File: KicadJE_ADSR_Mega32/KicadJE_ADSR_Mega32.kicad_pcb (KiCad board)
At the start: 2 copper layers, 100 x 100 mm, 212 parts, among them J101 ADSR1, J102 ADSR2, J103 ADSR1, J104 ADSR2, J105 ADSR1-G8, J106 ADSR2-G8, J107 ADSR4-G8, J108 ADSR3-G8, J201 AVR-ISP-6, J202 UART, J301 In, J302 +5V reg/doepfer, J303 Out, J304 CV_time, J305 CV doepfer, J401 CV, J402 FM, J403 Trigger, J404 Out, J405 SQ Out, J406 Sine Out, P101 Doepfer_Power_16pin, P302 Doepfer_Power_16pin, P401 Doepfer_Power_16pin, Q301 BC337, Q302 PZT2222A, Q401 UMX1N, Q402 MMBT2222A, Q403 MMBT2222A, Q404 MMBT2222A, Q405 MMBT2222A, SW401 LFO, SW402 SQ_Source, U201 ATmega32A-AU, U301 L78L05_TO92, U302 PT2399, U401 TL074, U402 74HC00, U403 TL072, Y201 16MHz

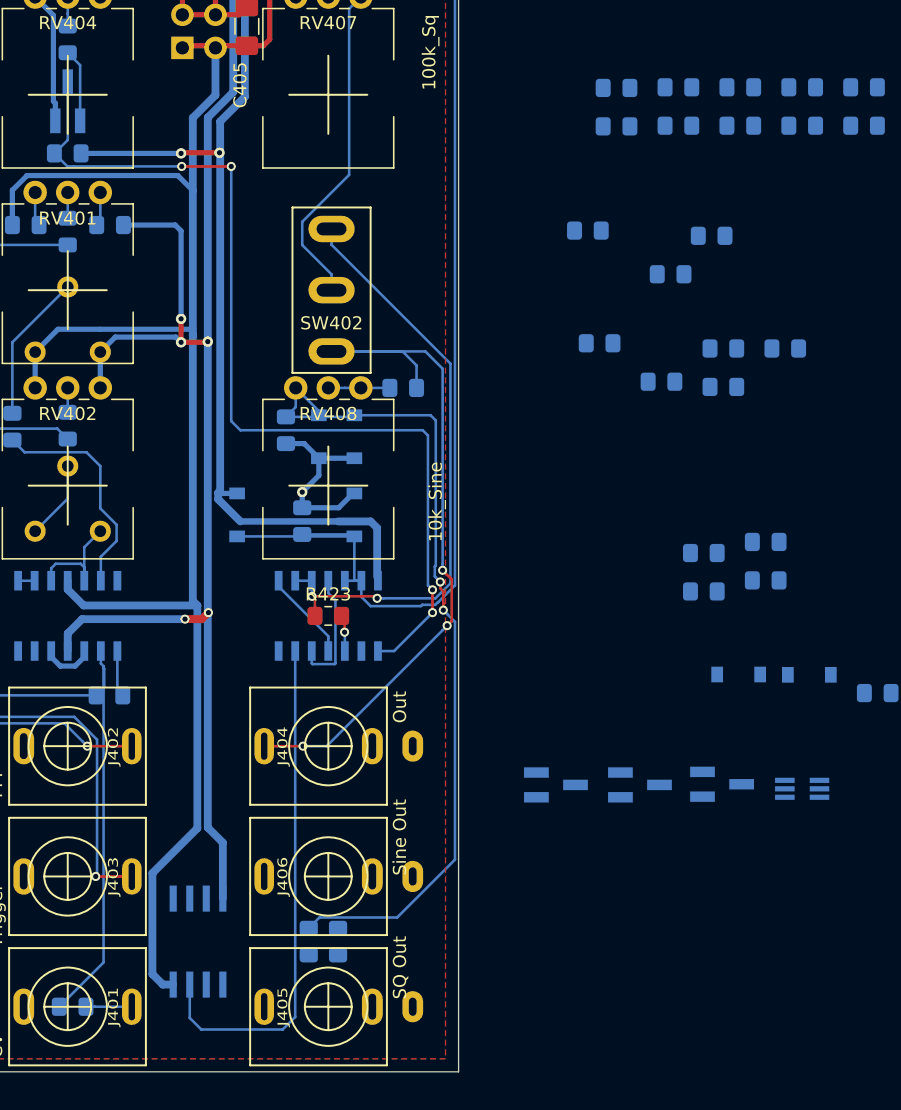
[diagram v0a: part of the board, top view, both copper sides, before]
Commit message: Square out - and decoupling
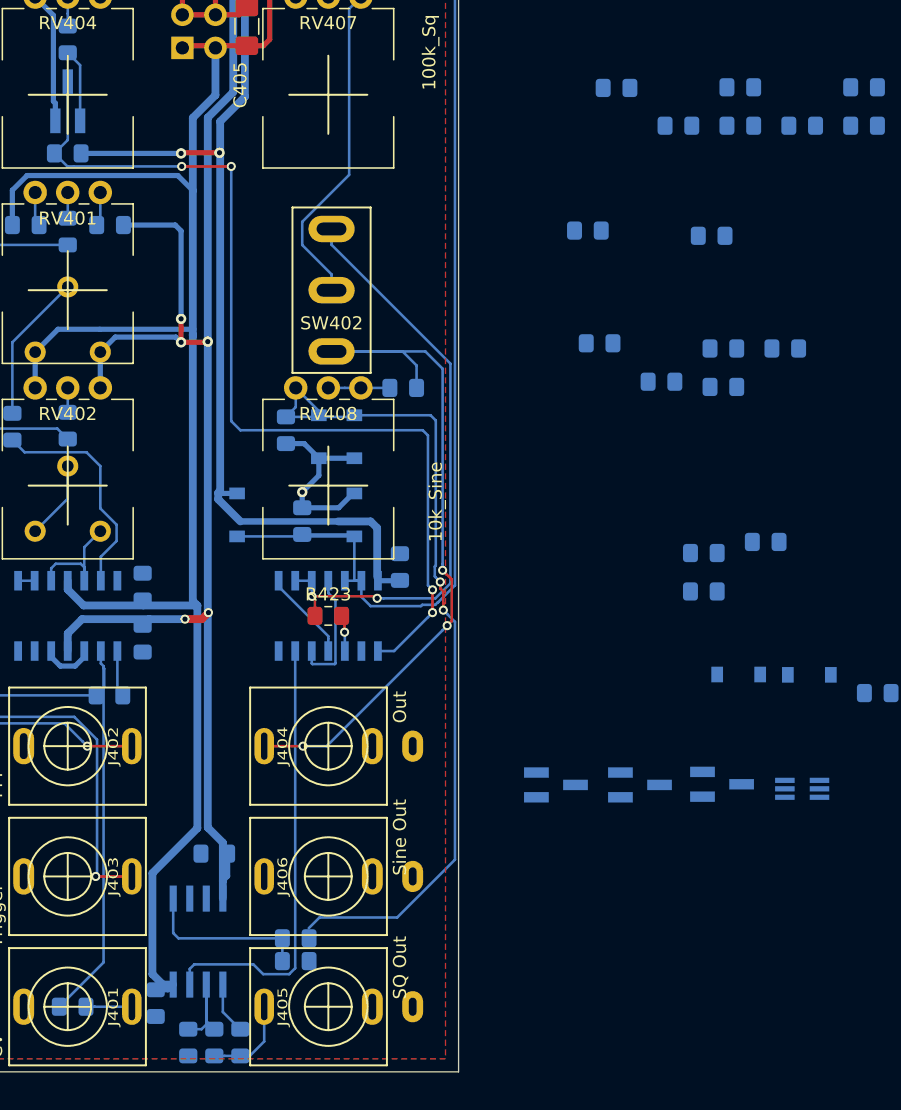
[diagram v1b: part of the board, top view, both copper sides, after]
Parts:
- added C412: 100n, Capacitor_SMD:C_0805_2012Metric_Pad1.15x1.40mm_HandSolder, B.Cu at (131.2, 133.2)
- added C413: 100n, Capacitor_SMD:C_0805_2012Metric_Pad1.15x1.40mm_HandSolder, B.Cu at (126.8, 144.7)
- added R435: 10k, Resistor_SMD:R_0805_2012Metric_Pad1.15x1.40mm_HandSolder, B.Cu at (131.2, 147.8)
- R416: value 4k7 -> 10k
- RV405: value 10k_offset -> 10k_Offset_out
- moved R426 85.1 mm to (133.2, 147.8), turned to 90 degrees
- moved R416 82.4 mm to (129.2, 147.8), turned to 90 degrees
- moved C408 53.6 mm to (125.8, 116.8), turned to 90 degrees
- moved C406 47.8 mm to (125.8, 112.8), turned to 270 degrees
- moved C404 30.6 mm to (145.5, 111.2), turned to 270 degrees
- moved R433 3.58 mm to (137.5, 141.5), turned to 180 degrees
- moved R432 1.03 mm to (137.5, 139.8), turned to 180 degrees
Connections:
- R416 pad 1: Net-(R416-Pad1) -> GNDA
- R416 pad 2: VCO_SQ_Out -> Net-(R416-Pad2)
- U403 pad 2: Net-(R416-Pad1) -> Net-(R416-Pad2)
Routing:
- net Net-(R432-Pad2): track 0.00 -> 12.9 mm
- net Net-(R416-Pad2): track 0.00 -> 8.28 mm
- net VCO_SQ_Out: track 0.00 -> 6.96 mm
- net Net-(U402-Pad6): track 39.5 -> 34.3 mm
- net Net-(R426-Pad2): track 0.00 -> 4.03 mm
- net +12V: track 129.1 -> 132.1 mm
- net -12V: track 150.3 -> 152.2 mm
- net +5VA: track 125.5 -> 127.2 mm

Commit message: Most of the oscillator
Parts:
- Q403, Q404, R420, R424: moved to F.Cu
- moved R419 70.8 mm to (115.2, 120.2), turned to 180 degrees
- moved Q401 63.7 mm to (114.0, 115.2), turned to 270 degrees
- moved C403 63.1 mm to (118.8, 120.2), turned to 180 degrees
- moved R424 54.3 mm to (137.0, 114.7), turned to 270 degrees
- moved R425 49.8 mm to (122.2, 110.5), turned to 180 degrees
- moved R421 48.3 mm to (145.5, 115.0), turned to 90 degrees
- moved R417 46.0 mm to (123.0, 120.2)
- moved D402 45.0 mm to (132.0, 117.5), turned to 270 degrees
- moved C402 43.3 mm to (125.8, 109.0), turned to 270 degrees
- moved D401 40.1 mm to (132.0, 112.8), turned to 270 degrees
- moved R420 35.1 mm to (135.2, 114.8), turned to 90 degrees
- moved Q404 32.2 mm to (139.5, 118.2)
- moved Q403 31.5 mm to (134.0, 118.2)
- moved Q405 20.5 mm to (154.0, 107.8)
- moved C409 19.6 mm to (154.5, 104.2), turned to 180 degrees
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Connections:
- C406 pad 1: GND -> GNDA
- C408 pad 1: GND -> GNDA
- C412 pad 1: GND -> GNDA
- C413 pad 1: GND -> GNDA
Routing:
- net GNDA: track 115.9 -> 153.0 mm, vias 15 -> 23
- net /AJ_VCO_Formant/b1: track 0.00 -> 21.0 mm
- net Net-(D401-Pad2): track 0.00 -> 19.0 mm, vias 0 -> 2
- net /AJ_VCO_Formant/c1: track 0.00 -> 16.1 mm
- net +5VA: track 127.2 -> 141.5 mm, vias 2 -> 3
- net Net-(Q404-Pad3): track 0.00 -> 7.49 mm, vias 0 -> 1
- net /AJ_VCO_Formant/e1: track 0.00 -> 7.48 mm
- net Net-(R425-Pad2): track 1.27 -> 6.34 mm
- net VCO_Exp: track 9.09 -> 13.6 mm
- net Net-(Q403-Pad3): track 0.00 -> 4.34 mm
- net Net-(C403-Pad2): track 0.00 -> 4.14 mm
- net Net-(Q404-Pad1): track 0.00 -> 4.01 mm
- net Net-(R413-Pad2): track 3.57 -> 7.52 mm
- net Net-(C402-Pad1): track 17.4 -> 21.1 mm
- net Net-(C402-Pad2): track 0.00 -> 3.37 mm
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
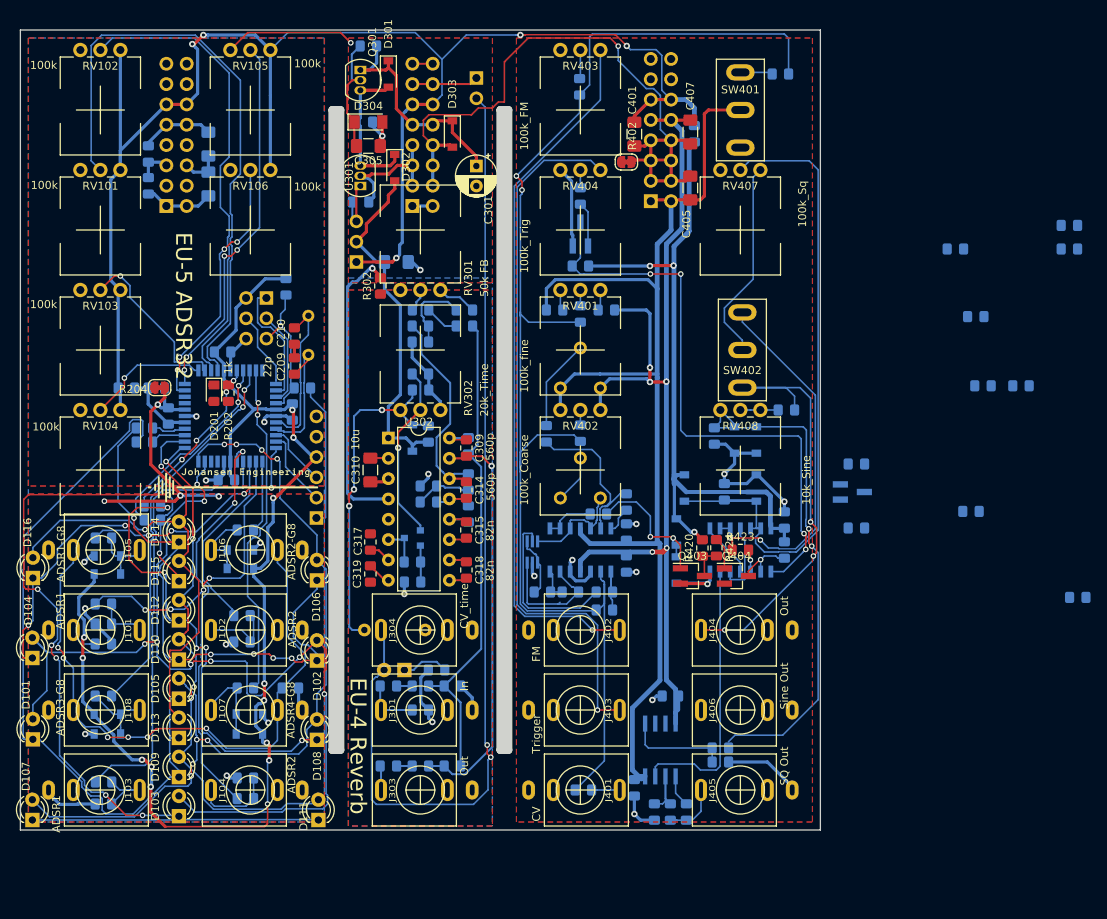
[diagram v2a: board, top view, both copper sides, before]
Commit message: Oscillator done
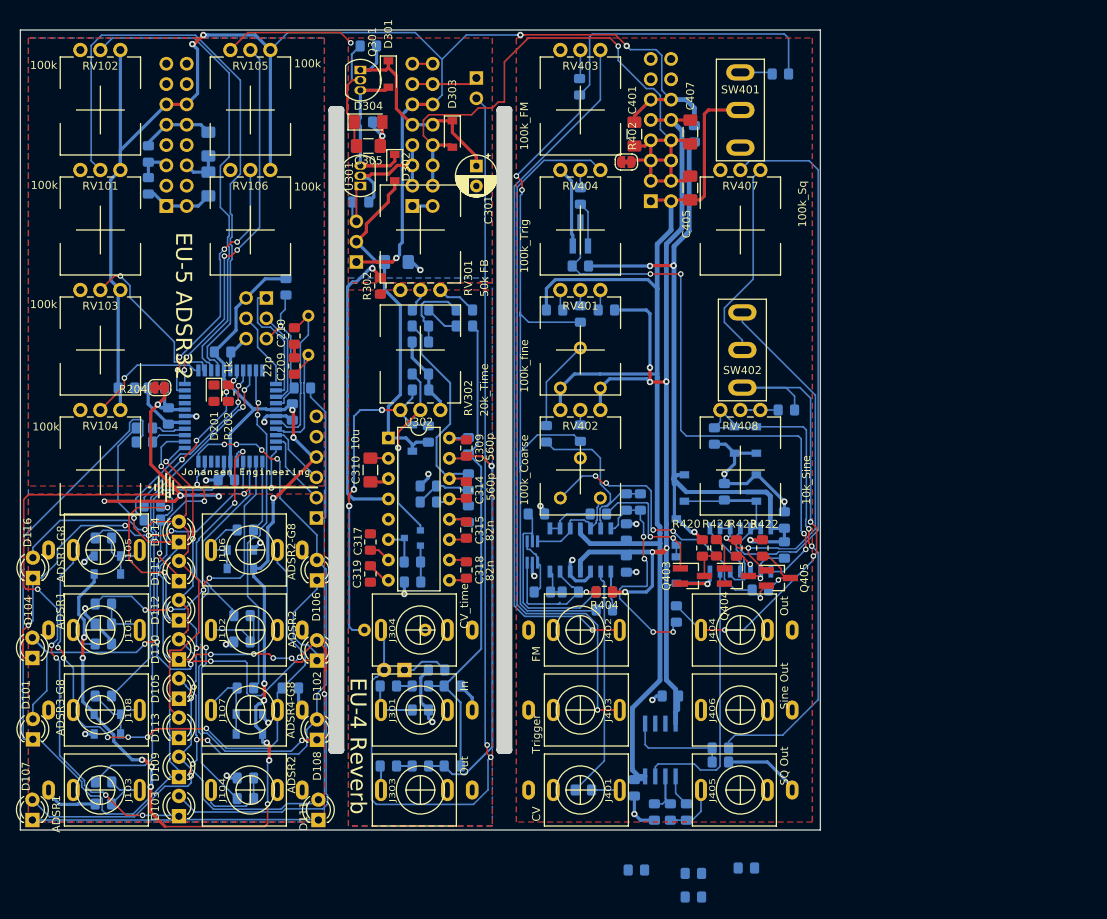
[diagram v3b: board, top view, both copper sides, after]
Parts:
- Q405, R404, R422: moved to F.Cu
- moved R430 93.6 mm to (134.1, 155.4)
- moved R428 93.6 mm to (134.1, 158.4)
- moved R431 69.4 mm to (140.8, 154.8)
- moved C411 61.3 mm to (127.0, 155.0)
- moved R418 60.2 mm to (114.5, 110.5), turned to 180 degrees
- moved R404 59.2 mm to (123.0, 120.2), turned to 180 degrees
- moved R415 50.5 mm to (127.5, 109.0), turned to 270 degrees
- moved R427 47.8 mm to (132.0, 123.0), turned to 270 degrees
- moved C409 19.8 mm to (142.5, 120.0)
- moved Q405 14.2 mm to (144.8, 118.5)
- moved R422 12.0 mm to (142.8, 114.8), turned to 90 degrees
- moved R423 0.56 mm to (139.5, 114.8), turned to 270 degrees
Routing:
- net Net-(C409-Pad2): track 6.04 -> 40.7 mm, vias 0 -> 5
- net Net-(C402-Pad2): track 3.37 -> 29.5 mm, vias 0 -> 4
- net +12V: track 132.1 -> 141.6 mm, vias 5 -> 6
- net Net-(C409-Pad1): track 0.00 -> 8.57 mm, vias 0 -> 1
- net +5VA: track 141.5 -> 147.4 mm, vias 3 -> 4
- net VCO_Nand: track 47.1 -> 52.2 mm
- net VCO_Out: track 56.1 -> 60.5 mm
- net /AJ_VCO_Formant/b1: track 21.0 -> 24.6 mm
- net Net-(C410-Pad1): track 85.6 -> 89.0 mm
- net /AJ_VCO_Formant/c1: track 16.1 -> 18.3 mm, vias 0 -> 1
- net Net-(C402-Pad1): track 21.1 -> 22.8 mm
- net GNDA: track 153.0 -> 154.3 mm, vias 23 -> 24
- net Net-(Q404-Pad3): track 7.49 -> 6.72 mm
- net Net-(D401-Pad2): track 19.0 -> 19.7 mm

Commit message: VCO routed
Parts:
- moved R428 23.7 mm to (137.7, 135.0), turned to 180 degrees
- moved R430 22.5 mm to (137.7, 133.2)
- moved C411 21.2 mm to (137.8, 136.8)
- moved R431 16.5 mm to (137.8, 138.5)
- moved R432 0.79 mm to (137.8, 140.5)
- moved R433 0.78 mm to (137.7, 142.2)
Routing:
- net Net-(R430-Pad2): track 0.00 -> 13.8 mm, vias 0 -> 2
- net VCO_SIN_Out: track 0.00 -> 5.16 mm
- net Net-(C411-Pad2): track 0.00 -> 3.51 mm
- net Net-(U402-Pad6): track 34.3 -> 35.7 mm
- net GNDA: track 154.3 -> 155.5 mm, vias 24 -> 25
- net Net-(R432-Pad2): track 12.9 -> 13.8 mm

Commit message: Update KicadJE_ADSR_Mega32.kicad_pcb
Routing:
- net Net-(C411-Pad2): track 3.51 -> 19.0 mm, vias 0 -> 2
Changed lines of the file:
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@@
     (thickness 1.6)
     (drawings 35)
-    (tracks 1978)
+    (tracks 1986)
     (zones 0)
     (modules 215)
@@
   (segment (start 138.775 136.75) (end 138.775 135.025) (width 0.2) (layer B.Cu) (net 130))
   (segment (start 138.775 136.75) (end 138.775 138.5) (width 0.2) (layer B.Cu) (net 130))
+  (via (at 140 139.5) (size 0.7) (drill 0.4) (layers F.Cu B.Cu) (net 130))
+  (segment (start 138.775 136.75) (end 138.775 138.275) (width 0.2) (layer B.Cu) (net 130))
+  (segment (start 138.775 138.275) (end 140 139.5) (width 0.2) (layer B.Cu) (net 130))
+  (via (at 135.5 139.5) (size 0.7) (drill 0.4) (layers F.Cu B.Cu) (net 130))
+  (segment (start 140 139.5) (end 135.5 139.5) (width 0.2) (layer F.Cu) (net 130))
+  (segment (start 129.365 137.425) (end 129.365 136.7) (width 0.2) (layer B.Cu) (net 130))
+  (segment (start 131.44 139.5) (end 129.365 137.425) (width 0.2) (layer B.Cu) (net 130))
+  (segment (start 135.5 139.5) (end 131.44 139.5) (width 0.2) (layer B.Cu) (net 130))
   (segment (start 128.095 139.345) (end 128.095 136.7) (width 0.2) (layer B.Cu) (net 131))
   (segment (start 130 141.25) (end 128.095 139.345) (width 0.2) (layer B.Cu) (net 131))

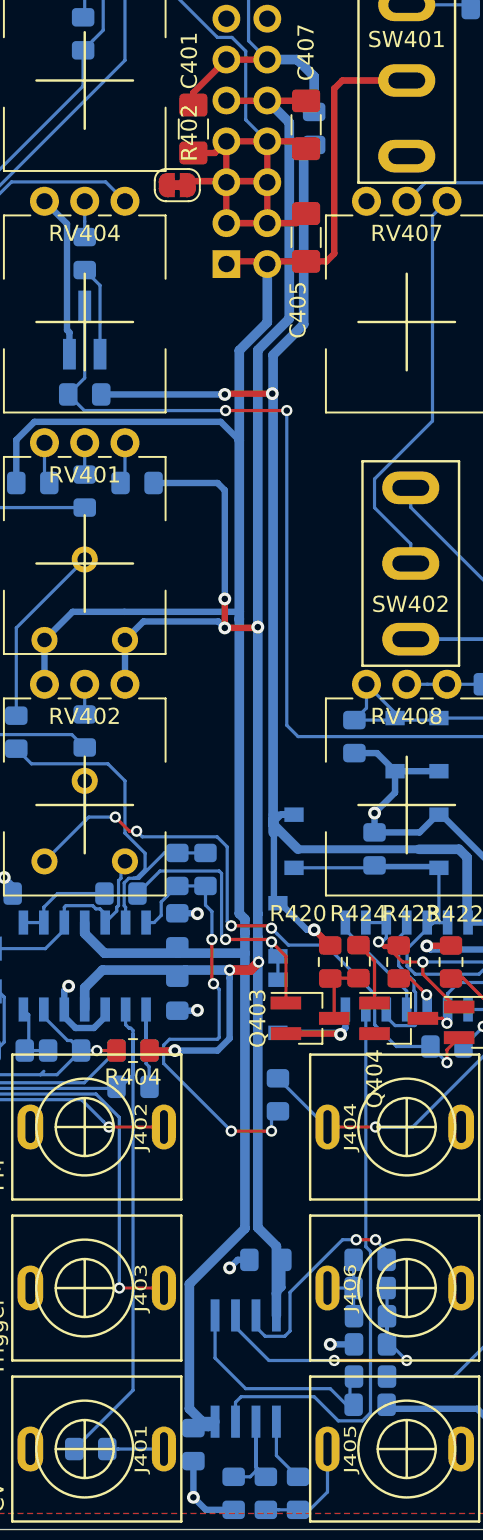
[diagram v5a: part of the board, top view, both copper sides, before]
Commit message: Label on VCO
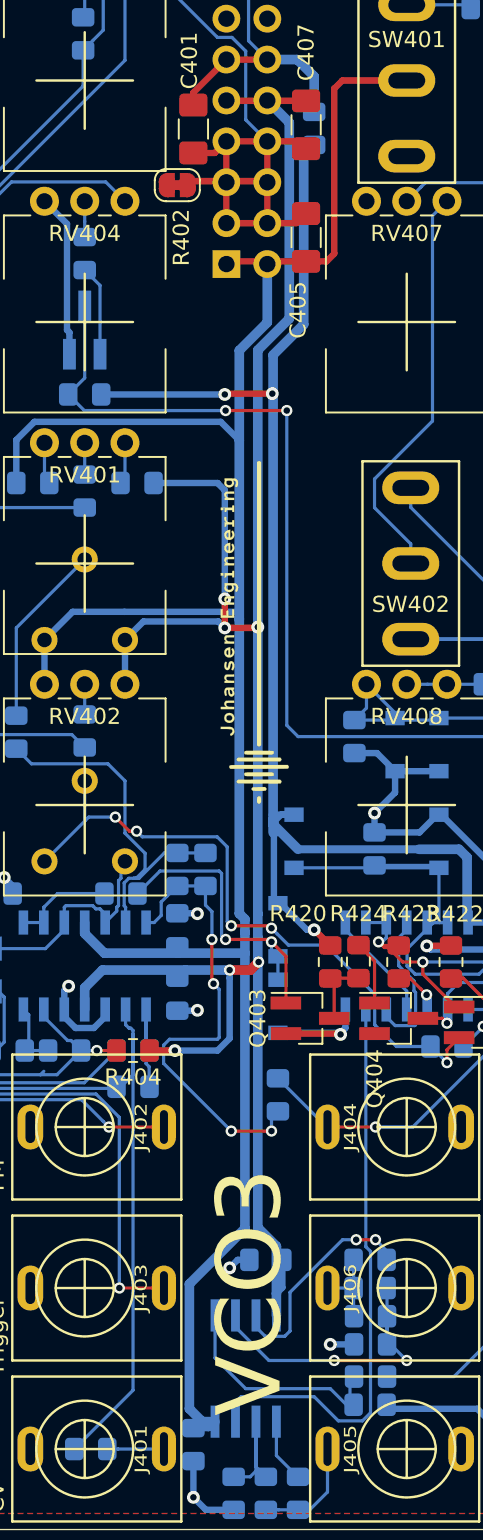
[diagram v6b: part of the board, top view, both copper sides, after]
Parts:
- added G***: LOGO, AJ:Johansen_engineering_logo_25mm_front_neg5, F.Cu at (130.8, 94.2)
- added G***: LOGO, AJ:Johansen_engineering_logo_25mm_front_neg5, B.Cu at (138.8, 82.5)
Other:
- board text added: "Johansen Engineering VCO3 Formant 2019 05 13"
- board text added: "VCO3"

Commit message: Gerber
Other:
- rule trace_min: 0.2 -> 0.15
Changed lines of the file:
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@@
     (32 B.Adhes user hide)
     (33 F.Adhes user hide)
-    (34 B.Paste user)
+    (34 B.Paste user hide)
     (35 F.Paste user hide)
     (36 B.SilkS user)
@@
     (44 Edge.Cuts user)
     (45 Margin user hide)
-    (46 B.CrtYd user hide)
-    (47 F.CrtYd user hide)
+    (46 B.CrtYd user)
+    (47 F.CrtYd user)
     (48 B.Fab user)
-    (49 F.Fab user)
+    (49 F.Fab user hide)
   )
   (setup
@@
     (zone_clearance 0.508)
     (zone_45_only no)
-    (trace_min 0.2)
+    (trace_min 0.15)
     (via_size 0.7)
     (via_drill 0.4)
@@
       (usegerberadvancedattributes false)
       (creategerberjobfile false)
-      (excludeedgelayer true)
-      (linewidth 0.100000)
+      (excludeedgelayer false)
+      (linewidth 0.150000)
       (plotframeref false)
       (viasonmask false)
@@
       (outputformat 1)
       (mirror false)
-      (drillshape 1)
+      (drillshape 0)
       (scaleselection 1)
-      (outputdirectory ""))
+      (outputdirectory "gerber_RevA"))
   )
   (net 0 "")
@@
     (attr smd)
     (fp_text reference R420 (at 3 -2 180) (layer F.SilkS)
-      (effects (font (size 1 1) (thickness 0.15)))
+      (effects (font (size 0.8 0.8) (thickness 0.15)))
     )
     (fp_text value 10k (at 0 1.65 90) (layer F.Fab)
@@
     (tags "resistor handsolder")
     (attr smd)
-    (fp_text reference R422 (at 2.975 0.25 180) (layer F.SilkS)
-      (effects (font (size 1 1) (thickness 0.15)))
+    (fp_text reference R422 (at 3 1.5 180) (layer F.SilkS)
+      (effects (font (size 0.8 0.8) (thickness 0.15)))
     )
     (fp_text value 10k (at 0 1.65 90) (layer F.Fab)
@@
     (attr smd)
     (fp_text reference R423 (at -3 -0.75) (layer F.SilkS)
-      (effects (font (size 1 1) (thickness 0.15)))
+      (effects (font (size 0.8 0.8) (thickness 0.15)))
     )
     (fp_text value 220R (at -0.25 -0.75 270) (layer F.Fab)
@@
     (attr smd)
     (fp_text reference R424 (at -2.975 0) (layer F.SilkS)
-      (effects (font (size 1 1) (thickness 0.15)))
+      (effects (font (size 0.8 0.8) (thickness 0.15)))
     )
     (fp_text value 1k (at 0 1.65 270) (layer F.Fab)
@@
     (tags "SOIC 1.27")
     (attr smd)
-    (fp_text reference U402 (at 0 5.375 90) (layer B.SilkS)
+    (fp_text reference U402 (at -0.25 -5.25 90) (layer B.SilkS)
       (effects (font (size 1 1) (thickness 0.15)) (justify mirror))
     )
